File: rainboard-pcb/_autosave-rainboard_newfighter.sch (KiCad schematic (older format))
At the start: 97 parts, among them J1 Conn_01x02, J10 Conn_01x03, J11 SDS-50J, J12 SDS-50J, J13 Conn_01x02, J14 Conn_01x02, J15 Conn_01x02, J16 Conn_01x02, J2 Conn_01x02, J3 Conn_01x02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

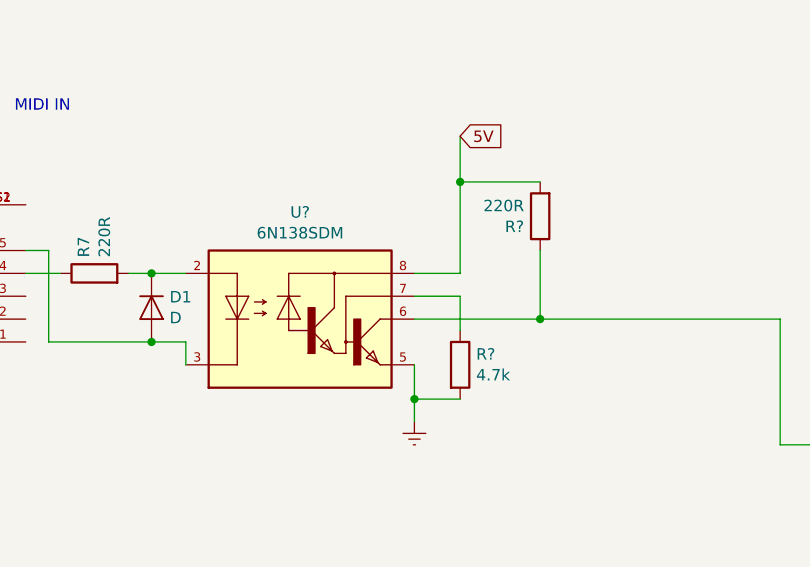
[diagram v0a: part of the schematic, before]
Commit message: Autorouted v0.4 with thicker power and earth traces
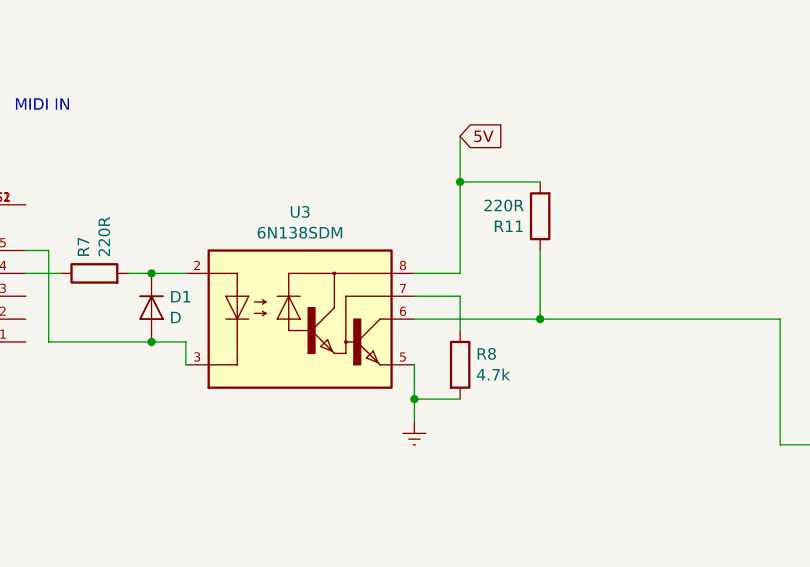
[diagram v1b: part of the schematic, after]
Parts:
- gave numbers to parts that had none: 3
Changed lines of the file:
@@
 	16000 11900 15800 11900
 $Comp
-L opto_couplers2:6N138SDM U?
+L opto_couplers2:6N138SDM U3
 U 1 1 5FAB76A0
 P 15300 12100
-F 0 "U?" H 15300 12567 50  0000 C CNN
+F 0 "U3" H 15300 12567 50  0000 C CNN
 F 1 "6N138SDM" H 15300 12476 50  0000 C CNN
 F 2 "opto_coupler2:COUPL_6N138SDM" H 15300 12100 50  0001 L BNN
@@
 	17400 12100 17400 12650
 $Comp
-L Device:R R?
+L Device:R R8
 U 1 1 5FD2967A
 P 16000 12300
-F 0 "R?" H 16070 12346 50  0000 L CNN
+F 0 "R8" H 16070 12346 50  0000 L CNN
 F 1 "4.7k" H 16070 12255 50  0000 L CNN
 F 2 "Resistor_SMD:R_0603_1608Metric" V 15930 12300 50  0001 C CNN
@@
 	15800 12450 15800 12550
 $Comp
-L Device:R R?
+L Device:R R11
 U 1 1 5FE16655
 P 16350 11650
-F 0 "R?" H 16420 11696 50  0000 L CNN
+F 0 "R11" H 16420 11696 50  0000 L CNN
 F 1 "220R" H 16420 11605 50  0000 L CNN
 F 2 "Resistor_SMD:R_0603_1608Metric" V 16280 11650 50  0001 C CNN
